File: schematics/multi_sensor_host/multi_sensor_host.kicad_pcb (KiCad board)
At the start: 4 copper layers, 169 parts, among them J1 left hand 0, J10 swd, J11 stm_boot, J13 right hand 0, J14 right hand 1, J15 right hand 2, J16 right hand 3, J17 rst_mcu, J18 left hand 3, J19 left leg 0, J2 left hand 1, J20 left leg 1, J21 right lef 0, J22 right leg 1, J3 bm_cfg, J4 left hand 2, J5 tx, J6 MY_USB_B, J7 rst_bm71, J8 rx, J9 uart1, U1 TCA9548A_TSSOP, U11 MCP111, U12 BM71BLES1FC2-0B02AA, U2 TCA9548A_TSSOP, U3 TCA9548A_TSSOP, U4 MCP111, U5 TPS79333-EP, U8 MCP73812, U9 MCP1603, Y1 Crystal

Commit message: a
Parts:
- moved C5 16.6 mm to (116.7, 78.8), turned to 90 degrees
- moved U5 12.5 mm to (120.0, 78.6), turned to 0 degrees
- moved C35 11.2 mm to (119.9, 81.6), turned to 180 degrees
- moved C80 8.68 mm to (123.2, 78.8), turned to -90 degrees
- moved D6 7.91 mm to (118.0, 102.0)
- moved R89 7.91 mm to (114.5, 103.3)
- moved C18 6.89 mm to (125.2, 78.8), turned to -90 degrees
- moved R98 5.53 mm to (128.2, 74.4), turned to 180 degrees
- moved R86 5.01 mm to (138.7, 64.5)
- moved C22 5.01 mm to (138.7, 67.8)
- moved J3 5.01 mm to (136.0, 65.0)
- moved D3 4.33 mm to (118.0, 95.0)
- moved R90 4.33 mm to (114.5, 96.2)
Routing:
- net GND: track 0.00 -> 442.5 mm, vias 0 -> 13
- net /stm_tx: track 0.00 -> 45.4 mm
- net /batt_charge_en: track 0.00 -> 40.9 mm, vias 0 -> 2
- net VCC: track 0.00 -> 38.7 mm
- net /stm_rx: track 0.00 -> 33.2 mm
- net /Vbus: track 0.00 -> 26.4 mm, vias 0 -> 1
- net /usb_d+: track 0.00 -> 20.1 mm
- net /usb_d-: track 0.00 -> 17.5 mm
- net /bm_cfg: track 0.00 -> 16.6 mm
- net /clk-in: track 0.00 -> 11.8 mm
- net /batt_sense: track 0.00 -> 11.0 mm
- net /Vbatt: track 0.00 -> 10.1 mm
- net VDD: track 0.00 -> 7.96 mm
- net /uart1-tx: track 0.00 -> 7.93 mm
- net /led-0: track 0.00 -> 7.61 mm, vias 0 -> 1
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
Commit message: a
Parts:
- moved R86 8.04 mm to (135.8, 72.0), turned to 0 degrees
- moved C22 3.79 mm to (135.8, 70.2), turned to 180 degrees
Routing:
- net GND: track 442.5 -> 586.8 mm, vias 13 -> 15
- net /rst_bm71: track 0.00 -> 85.5 mm
- net VCC: track 38.7 -> 111.4 mm, vias 0 -> 2
- net VDD: track 7.96 -> 74.3 mm, vias 0 -> 1
- net /Vin: track 6.01 -> 62.2 mm, vias 0 -> 1
- net /Vbatt: track 10.1 -> 63.5 mm, vias 0 -> 1
- net /Vbus: track 26.4 -> 36.3 mm
- net /bm_rx: track 4.66 -> 8.97 mm
- net /bm_cfg: track 16.6 -> 19.9 mm
- net Net-(U9-Lx): track 0.00 -> 2.84 mm
- net /boot0: track 0.00 -> 2.64 mm
- net /stm_rx: track 33.2 -> 34.8 mm
- net /stm_tx: track 45.4 -> 44.8 mm

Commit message: a
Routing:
- net VDD: track 74.3 -> 336.6 mm, vias 1 -> 11
- net GND: track 586.8 -> 779.3 mm, vias 15 -> 33
- net /rst_mcu: track 0.00 -> 106.8 mm
- net /led-1: track 0.00 -> 14.1 mm, vias 0 -> 2
- net /led-0: track 7.61 -> 20.6 mm, vias 1 -> 2
- net /swd_io: track 0.00 -> 12.0 mm
- net /led-2: track 0.00 -> 9.24 mm, vias 0 -> 2
- net /boot0: track 2.64 -> 9.33 mm
- net /swd_clk: track 0.00 -> 4.97 mm
- net /sda_host_b: track 0.00 -> 4.63 mm
- net Net-(U10B-Vcap_1): track 0.00 -> 4.24 mm
- net /Vin: track 62.2 -> 66.3 mm
- net Net-(D4-K): track 0.00 -> 3.76 mm
- net /sda_host_c: track 0.00 -> 3.74 mm
- net Net-(D6-K): track 0.00 -> 3.71 mm
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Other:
- board outline added: 76 x 105.5 mm

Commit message: a
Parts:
- turned R18 to 180 degrees
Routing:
- net VDD: track 336.6 -> 729.3 mm, vias 11 -> 23
- net /scl_host_b: track 2.90 -> 67.7 mm, vias 0 -> 2
- net /sda_host_b: track 4.63 -> 66.2 mm, vias 0 -> 2
- net /sda_host_c: track 3.74 -> 51.1 mm, vias 0 -> 2
- net /scl_host_c: track 3.18 -> 47.0 mm, vias 0 -> 2
- net /scl_host_a: track 2.82 -> 45.8 mm, vias 0 -> 2
- net GND: track 779.3 -> 820.0 mm, vias 33 -> 45
- net /sda_host_a: track 3.19 -> 43.7 mm, vias 0 -> 2

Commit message: a
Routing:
- net VDD: track 729.3 -> 994.6 mm, vias 23 -> 25
- net GND: track 820.0 -> 910.9 mm
- net /scl_23: track 0.00 -> 54.3 mm, vias 0 -> 2
- net /sda_8: track 0.00 -> 44.6 mm, vias 0 -> 2
- net /scl_22: track 0.00 -> 42.9 mm, vias 0 -> 2
- net /sda_23: track 0.00 -> 42.0 mm, vias 0 -> 2
- net /scl_8: track 0.00 -> 40.7 mm, vias 0 -> 2
- net /sda_22: track 0.00 -> 40.4 mm, vias 0 -> 2
- net /scl_15: track 0.00 -> 39.6 mm, vias 0 -> 2
- net /sda_16: track 0.00 -> 38.4 mm, vias 0 -> 2
- net /scl_7: track 0.00 -> 37.5 mm, vias 0 -> 2
- net /scl_21: track 0.00 -> 35.9 mm, vias 0 -> 2
- net /sda_9: track 0.00 -> 35.8 mm, vias 0 -> 2
- net /scl_16: track 0.00 -> 35.5 mm, vias 0 -> 2
- net /sda_7: track 0.00 -> 33.5 mm, vias 0 -> 2
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
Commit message: a
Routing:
- net VDD: track 994.6 -> 1126.4 mm
- net /sda_2: track 0.00 -> 33.2 mm, vias 0 -> 2
- net /scl_2: track 0.00 -> 33.2 mm, vias 0 -> 2
- net /sda_3: track 0.00 -> 30.8 mm, vias 0 -> 2
- net /scl_5: track 0.00 -> 28.9 mm, vias 0 -> 2
- net /scl_3: track 0.00 -> 28.8 mm, vias 0 -> 2
- net /sda_5: track 0.00 -> 25.6 mm, vias 0 -> 2
- net /scl_4: track 0.00 -> 25.5 mm, vias 0 -> 2
- net /sda_4: track 0.00 -> 23.9 mm, vias 0 -> 1
- net /sda_6: track 8.07 -> 31.3 mm, vias 1 -> 2
- net /scl_6: track 32.7 -> 33.7 mm

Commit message: I think, I've finished it.
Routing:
- net /sda_0: track 0.00 -> 46.8 mm, vias 0 -> 2
- net /scl_0: track 0.00 -> 43.4 mm, vias 0 -> 2
- net /sda_1: track 0.00 -> 39.5 mm, vias 0 -> 2
- net /scl_1: track 0.00 -> 37.2 mm, vias 0 -> 2
- net VDD: track 1126.4 -> 1156.5 mm
- net /Vbatt: track 64.9 -> 61.5 mm
- net GND: track 910.9 -> 913.8 mm
- net /Vin: track 66.3 -> 64.9 mm
- net /sda_host_b: track 66.4 -> 65.8 mm
- added copper zone on B.Cu, net GND
- added copper zone on F.Cu, net GND
- added copper zone on In1.Cu, net GND
- added copper zone on In2.Cu, net VCC
- added copper zone on In2.Cu, net VDD

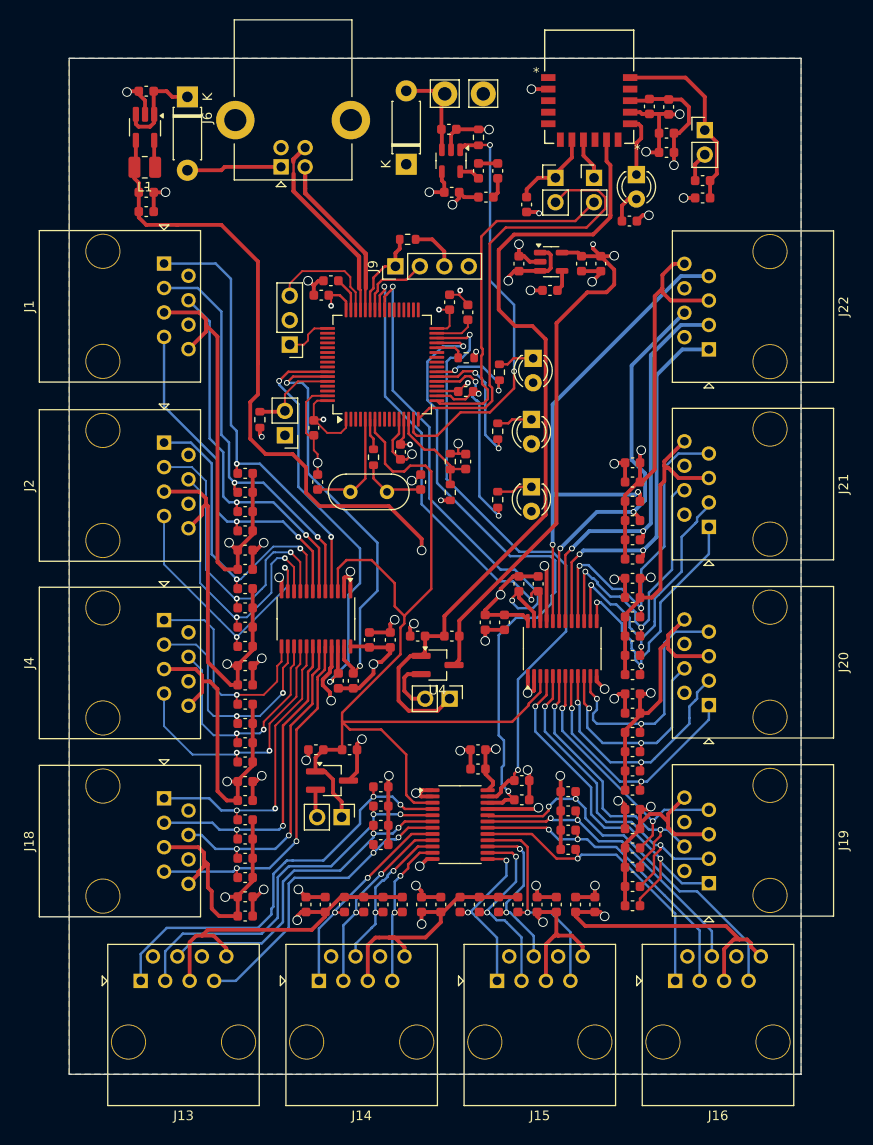
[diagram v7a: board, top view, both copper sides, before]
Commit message: A ground with vias as recommended by the BM71 manual.
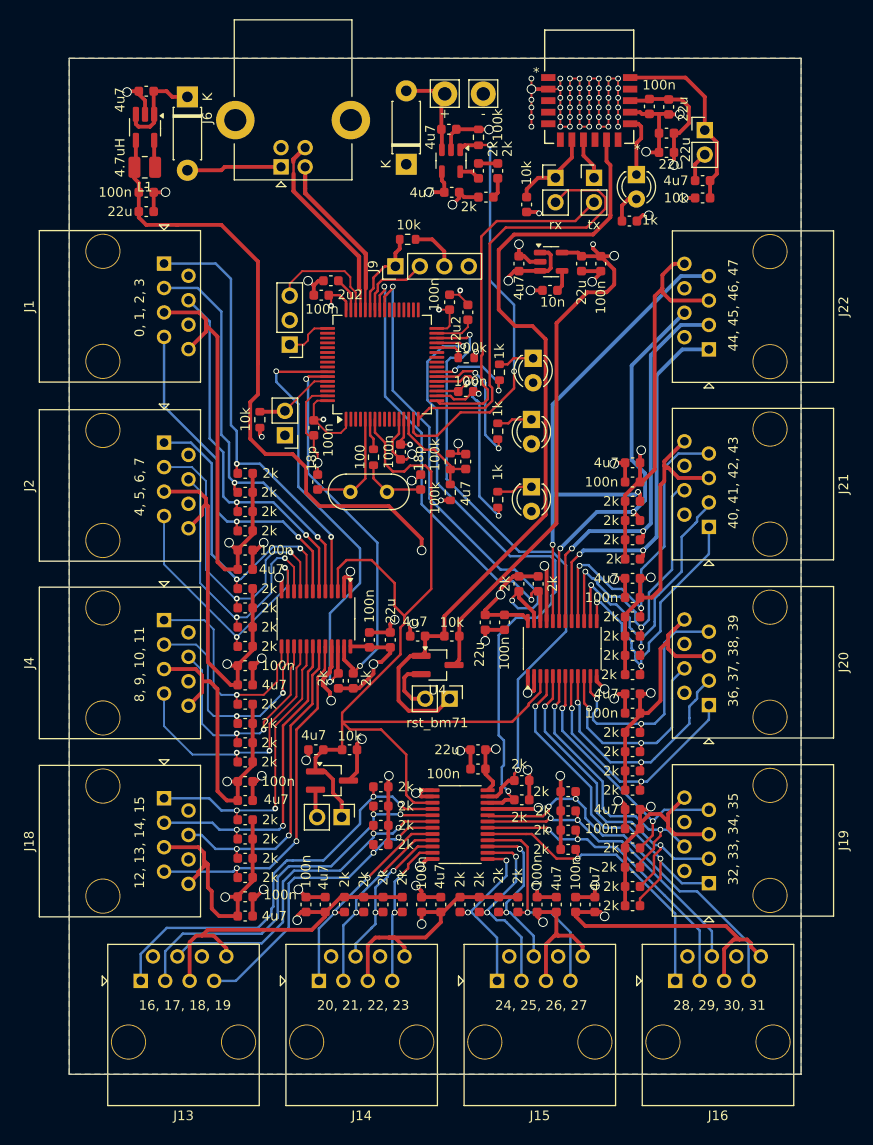
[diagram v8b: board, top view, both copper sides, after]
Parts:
- J1: value left hand 0 -> 0, 1, 2, 3
- J13: value right hand 0 -> 16, 17, 18, 19
- J14: value right hand 1 -> 20, 21, 22, 23
- J15: value right hand 2 -> 24, 25, 26, 27
- J16: value right hand 3 -> 28, 29, 30, 31
- J18: value left hand 3 -> 12, 13, 14, 15
- J19: value left leg 0 -> 32, 33, 34, 35
- J2: value left hand 1 -> 4, 5, 6, 7
- J20: value left leg 1 -> 36, 37, 38, 39
- J21: value right lef 0 -> 40, 41, 42, 43
- J22: value right leg 1 -> 44, 45, 46, 47
- J4: value left hand 2 -> 8, 9, 10, 11
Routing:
- net GND: track 913.8 -> 961.1 mm, vias 45 -> 92
- net /sda_host_a: track 43.7 -> 40.2 mm
- net /scl_host_a: track 45.6 -> 46.7 mm
- net /boot0: track 9.33 -> 8.33 mm
